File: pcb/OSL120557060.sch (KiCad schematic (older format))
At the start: 80 parts, among them J1 USB_C_Plug_USB2.0, J2 USB_C_Plug_USB2.0, J3 AVR-ISP-6, SW1 SW_SPST, SW10 SW_SPST, SW11 SW_SPST, SW12 SW_SPST, SW13 SW_SPST, SW14 SW_SPST, SW15 SW_SPST, SW16 SW_SPST, SW17 SW_SPST, SW18 SW_SPST, SW19 SW_SPST, SW2 SW_SPST, SW20 SW_SPST, SW21 SW_SPST, SW22 SW_SPST, SW23 SW_SPST, SW24 SW_SPST, SW25 SW_SPST, SW26 SW_SPST, SW27 SW_SPST, SW28 SW_SPST, SW29 SW_SPST, SW3 SW_SPST, SW30 SW_SPST, SW4 SW_SPST, SW5 SW_SPST, SW6 SW_SPST, SW7 SW_SPST, SW8 SW_SPST, SW9 SW_SPST, U1 ATmega328-PU, X1 16MHz

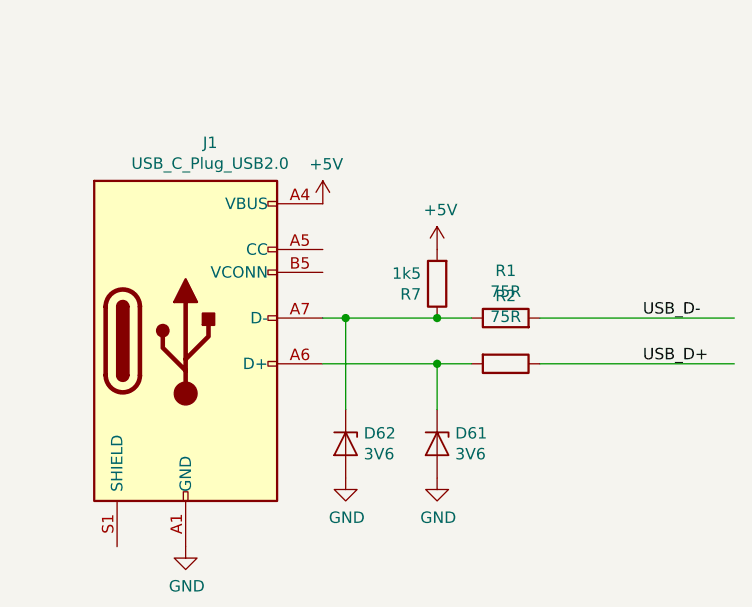
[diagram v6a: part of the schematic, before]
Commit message: * added pulldown resistors to allow usb-c usb-c cables * fixed usb-c footprint for reversibility
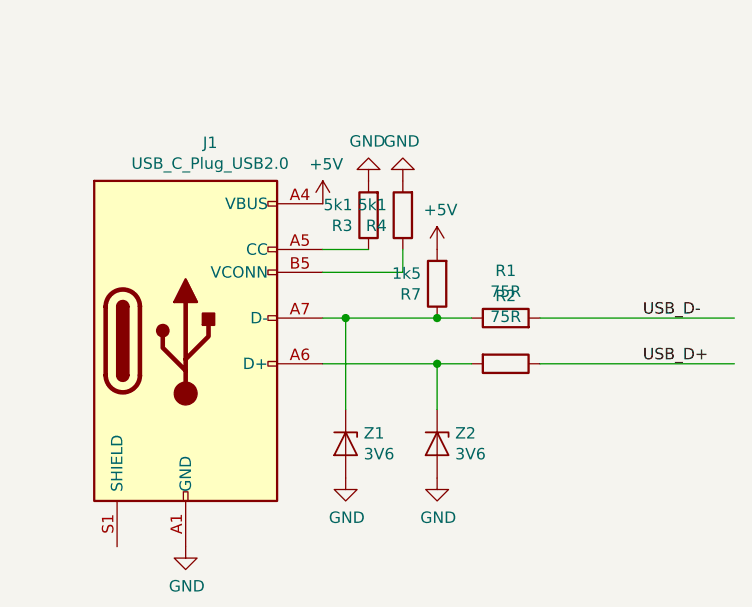
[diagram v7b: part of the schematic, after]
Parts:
- added R3, R4: 5k1, Resistor_THT:R_Axial_DIN0207_L6.3mm_D2.5mm_P7.62mm_Horizontal, symbol Device:R
- renumbered D62 to Z1, D61 to Z2
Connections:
- wire segments 123 -> 126
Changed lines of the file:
@@
 	10150 2400 11000 2400
 $Comp
-L Device:D_Zener D62
+L Device:D_Zener Z1
 U 1 1 5D157151
 P 9300 2750
-F 0 "D62" V 9254 2829 50  0000 L CNN
+F 0 "Z1" V 9254 2829 50  0000 L CNN
 F 1 "3V6" V 9345 2829 50  0000 L CNN
 F 2 "Diode_THT:D_T-1_P5.08mm_Horizontal" H 9300 2750 50  0001 C CNN
@@
 $EndComp
 $Comp
-L Device:D_Zener D61
+L Device:D_Zener Z2
 U 1 1 5D1584AC
 P 9700 2750
-F 0 "D61" V 9654 2829 50  0000 L CNN
+F 0 "Z2" V 9654 2829 50  0000 L CNN
 F 1 "3V6" V 9745 2829 50  0000 L CNN
 F 2 "Diode_THT:D_T-1_P5.08mm_Horizontal" H 9700 2750 50  0001 C CNN
@@
 Wire Wire Line
 	10050 4550 11000 4550
+$Comp
+L Device:R R3
+U 1 1 5D24971F
+P 9400 1750
+F 0 "R3" H 9470 1796 50  0000 L CNN
+F 1 "5k1" H 9470 1705 50  0000 L CNN
+F 2 "Resistor_THT:R_Axial_DIN0207_L6.3mm_D2.5mm_P7.62mm_Horizontal" V 9330 1750 50  0001 C CNN
+F 3 "~" H 9400 1750 50  0001 C CNN
+	1    9400 1750
+	-1   0    0    1
+$EndComp
+$Comp
+L power:GND #PWR0108
+U 1 1 5D24E548
+P 9400 1600
+F 0 "#PWR0108" H 9400 1350 50  0001 C CNN
+F 1 "GND" H 9405 1427 50  0000 C CNN
+F 2 "" H 9400 1600 50  0001 C CNN
+F 3 "" H 9400 1600 50  0001 C CNN
+	1    9400 1600
+	-1   0    0    1
+$EndComp
+Wire Wire Line
+	9200 1900 9400 1900
+$Comp
+L Device:R R4
+U 1 1 5D25CFEA
+P 9550 1750
+F 0 "R4" H 9620 1796 50  0000 L CNN
+F 1 "5k1" H 9620 1705 50  0000 L CNN
+F 2 "Resistor_THT:R_Axial_DIN0207_L6.3mm_D2.5mm_P7.62mm_Horizontal" V 9480 1750 50  0001 C CNN
+F 3 "~" H 9550 1750 50  0001 C CNN
+	1    9550 1750
+	-1   0    0    1
+$EndComp
+$Comp
+L power:GND #PWR0114
+U 1 1 5D25CFF0
+P 9550 1600
+F 0 "#PWR0114" H 9550 1350 50  0001 C CNN
+F 1 "GND" H 9555 1427 50  0000 C CNN
+F 2 "" H 9550 1600 50  0001 C CNN
+F 3 "" H 9550 1600 50  0001 C CNN
+	1    9550 1600
+	-1   0    0    1
+$EndComp
+Wire Wire Line
+	9550 1900 9550 2000
+Wire Wire Line
+	9550 2000 9200 2000
 $EndSCHEMATC
